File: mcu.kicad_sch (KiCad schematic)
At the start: 0 parts

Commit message: add ethernet
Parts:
- added U?: STM32F429ZGTx, Package_QFP:LQFP-144_20x20mm_P0.5mm, symbol MCU_ST_STM32F4:STM32F429ZGTx
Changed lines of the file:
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@@
 (kicad_sch (version 20211123) (generator eeschema)
   (paper "A3")
+  (symbol (lib_id "MCU_ST_STM32F4:STM32F429ZGTx") (at 199.39 143.51 0) (unit 1)
+    (in_bom yes) (on_board yes) (fields_autoplaced)
+    (property "Reference" "U?" (id 0) (at 214.1094 232.41 0)
+      (effects (font (size 1.27 1.27)) (justify left))
+    )
+    (property "Value" "STM32F429ZGTx" (id 1) (at 214.1094 234.95 0)
+      (effects (font (size 1.27 1.27)) (justify left))
+    )
+    (property "Footprint" "Package_QFP:LQFP-144_20x20mm_P0.5mm" (id 2) (at 173.99 229.87 0)
+      (effects (font (size 1.27 1.27)) (justify right) hide)
+    )
+    (property "Datasheet" "http://www.st.com/st-web-ui/static/active/en/resource/technical/document/datasheet/DM00071990.pdf" (id 3) (at 199.39 143.51 0)
+      (effects (font (size 1.27 1.27)) hide)
+    )
+    (pin "1")
+    (pin "10")
+    (pin "100")
+    (pin "101")
+    (pin "102")
+    (pin "103")
+    (pin "104")
+    (pin "105")
+    (pin "106")
+    (pin "107")
+    (pin "108")
+    (pin "109")
+    (pin "11")
+    (pin "110")
+    (pin "111")
+    (pin "112")
+    (pin "113")
+    (pin "114")
+    (pin "115")
+    (pin "116")
+    (pin "117")
+    (pin "118")
+    (pin "119")
+    (pin "12")
+    (pin "120")
+    (pin "121")
+    (pin "122")
+    (pin "123")
+    (pin "124")
+    (pin "125")
+    (pin "126")
+    (pin "127")
+    (pin "128")
+    (pin "129")
+    (pin "13")
+    (pin "130")
+    (pin "131")
+    (pin "132")
+    (pin "133")
+    (pin "134")
+    (pin "135")
+    (pin "136")
+    (pin "137")
+    (pin "138")
+    (pin "139")
+    (pin "14")
+    (pin "140")
+    (pin "141")
+    (pin "142")
+    (pin "143")
+    (pin "144")
+    (pin "15")
+    (pin "16")
+    (pin "17")
+    (pin "18")
+    (pin "19")
+    (pin "2")
+    (pin "20")
+    (pin "21")
+    (pin "22")
+    (pin "23")
+    (pin "24")
+    (pin "25")
+    (pin "26")
+    (pin "27")
+    (pin "28")
+    (pin "29")
+    (pin "3")
+    (pin "30")
+    (pin "31")
+    (pin "32")
+    (pin "33")
+    (pin "34")
+    (pin "35")
+    (pin "36")
+    (pin "37")
+    (pin "38")
+    (pin "39")
+    (pin "4")
+    (pin "40")
+    (pin "41")
+    (pin "42")
+    (pin "43")
+    (pin "44")
+    (pin "45")
+    (pin "46")
+    (pin "47")
+    (pin "48")
+    (pin "49")
+    (pin "5")
+    (pin "50")
+    (pin "51")
+    (pin "52")
+    (pin "53")
+    (pin "54")
+    (pin "55")
+    (pin "56")
+    (pin "57")
+    (pin "58")
+    (pin "59")
+    (pin "6")
+    (pin "60")
+    (pin "61")
+    (pin "62")
+    (pin "63")
+    (pin "64")
+    (pin "65")
+    (pin "66")
+    (pin "67")
+    (pin "68")
+    (pin "69")
+    (pin "7")
+    (pin "70")
+    (pin "71")
+    (pin "72")
+    (pin "73")
+    (pin "74")
+    (pin "75")
+    (pin "76")
+    (pin "77")
+    (pin "78")
+    (pin "79")
+    (pin "8")
+    (pin "80")
+    (pin "81")
+    (pin "82")
+    (pin "83")
+    (pin "84")
+    (pin "85")
+    (pin "86")
+    (pin "87")
+    (pin "88")
+    (pin "89")
+    (pin "9")
+    (pin "90")
+    (pin "91")
+    (pin "92")
+    (pin "93")
+    (pin "94")
+    (pin "95")
+    (pin "96")
+    (pin "97")
+    (pin "98")
+    (pin "99")
+  )
 )

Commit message: add USB
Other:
- company: (none) -> M-Labs
- title: (none) -> Kirdy
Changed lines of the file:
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@@
 (kicad_sch (version 20211123) (generator eeschema)
   (paper "A3")
+  (title_block
+    (title "Kirdy")
+    (date "2022-07-03")
+    (rev "r0.1")
+    (company "M-Labs")
+    (comment 1 "Alex Wong Tat Hang")
+  )
   (symbol (lib_id "MCU_ST_STM32F4:STM32F429ZGTx") (at 199.39 143.51 0) (unit 1)
     (in_bom yes) (on_board yes) (fields_autoplaced)

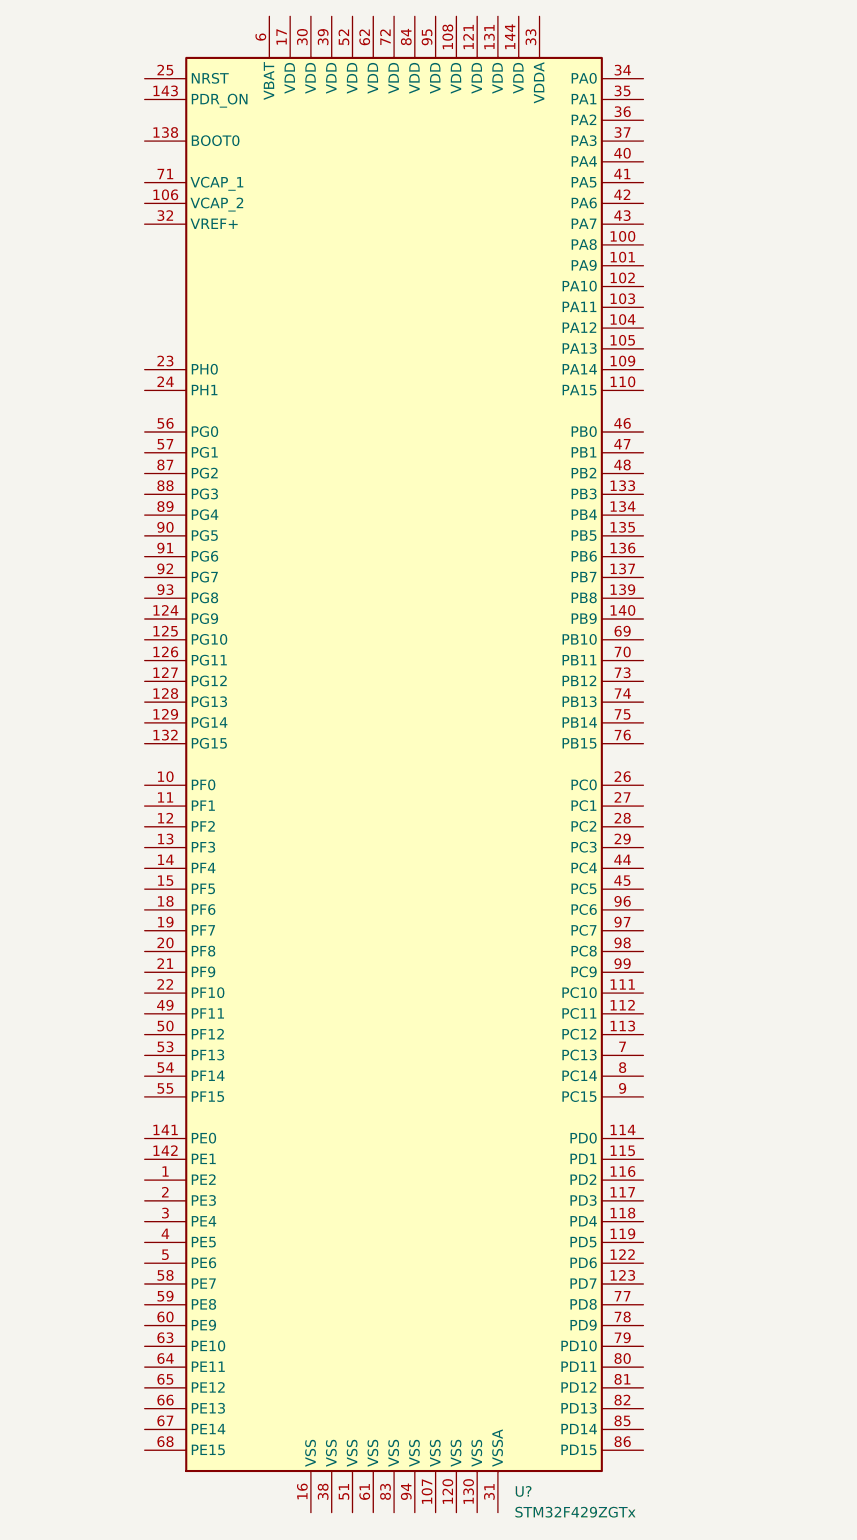
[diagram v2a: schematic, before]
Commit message: add MCU basic connections
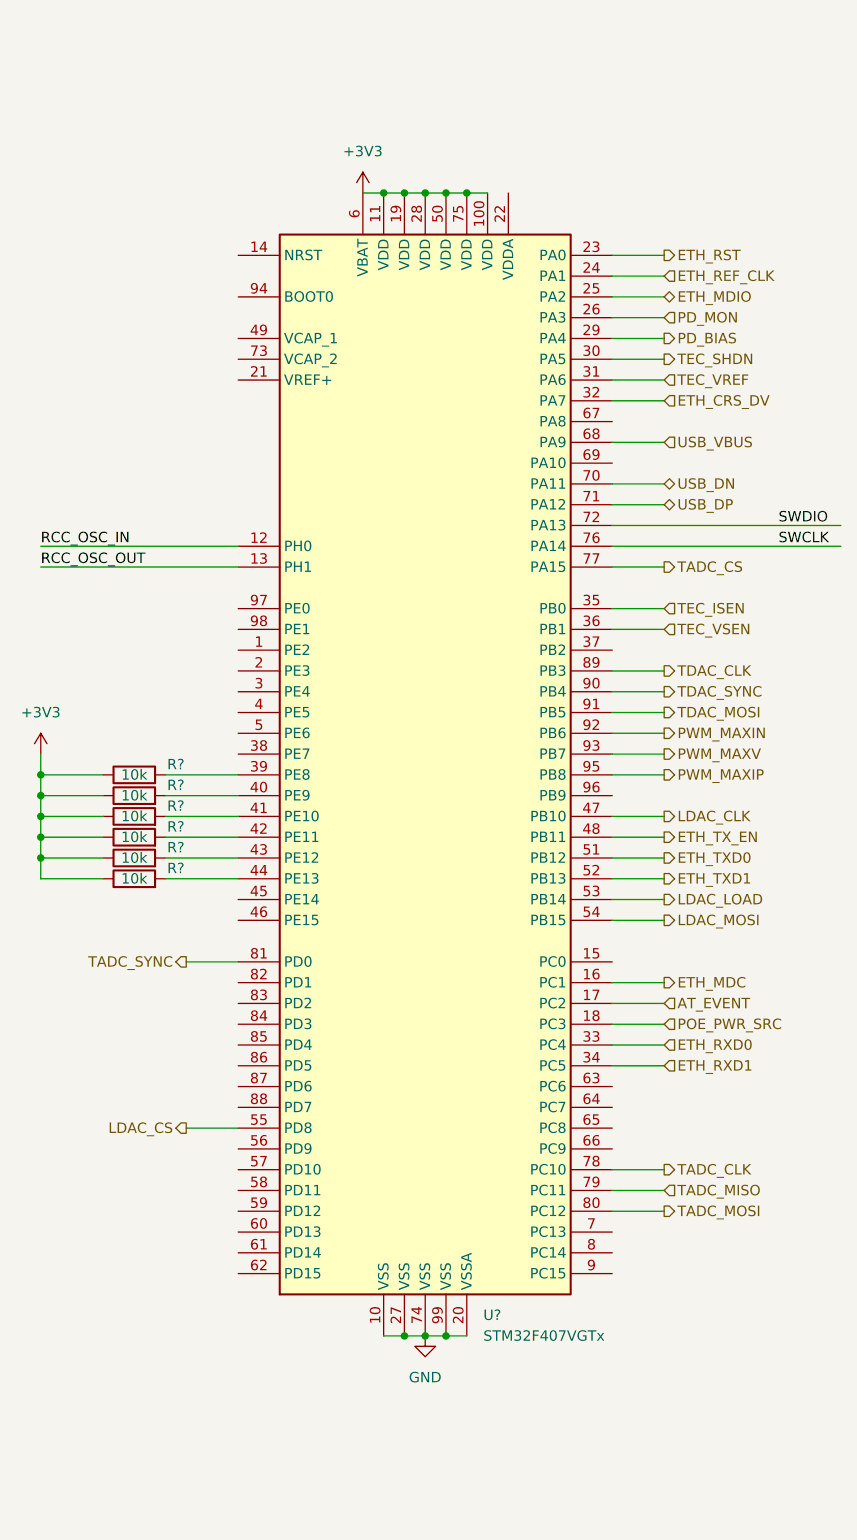
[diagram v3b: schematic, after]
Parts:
- removed U?: STM32F429ZGTx, Package_QFP:LQFP-144_20x20mm_P0.5mm, symbol MCU_ST_STM32F4:STM32F429ZGTx
- added R? (x6): 10k, symbol Device:R
- added U?: STM32F407VGTx, Package_QFP:LQFP-100_14x14mm_P0.5mm, symbol MCU_ST_STM32F4:STM32F407VGTx
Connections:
- new net: R?.2, U?.41 (PE10)
- new net: R?.2, U?.39 (PE8)
- new net: R?.2, U?.40 (PE9)
- new net: R?.2, U?.42 (PE11)
- new net: R?.2, U?.43 (PE12)
- new net: R?.2, U?.44 (PE13)
- new net +3V3: R?.1, R?.1, R?.1, R?.1, R?.1, R?.1, U?.100 (VDD), U?.11 (VDD), U?.19 (VDD), U?.28 (VDD), U?.50 (VDD), U?.6 (VBAT), U?.75 (VDD)
- new net AT_EVENT: U?.17 (PC2)
- new net ETH_CRS_DV: U?.32 (PA7)
- new net ETH_MDC: U?.16 (PC1)
- new net ETH_MDIO: U?.25 (PA2)
- new net ETH_REF_CLK: U?.24 (PA1)
- new net ETH_RST: U?.23 (PA0)
- new net ETH_RXD0: U?.33 (PC4)
- new net ETH_RXD1: U?.34 (PC5)
- new net ETH_TXD0: U?.51 (PB12)
- new net ETH_TXD1: U?.52 (PB13)
- new net ETH_TX_EN: U?.48 (PB11)
- new net GND: U?.10 (VSS), U?.20 (VSSA), U?.27 (VSS), U?.74 (VSS), U?.99 (VSS)
- new net LDAC_CLK: U?.47 (PB10)
- new net LDAC_CS: U?.55 (PD8)
- new net LDAC_LOAD: U?.53 (PB14)
- new net LDAC_MOSI: U?.54 (PB15)
- new net PD_BIAS: U?.29 (PA4)
- new net PD_MON: U?.26 (PA3)
- new net POE_PWR_SRC: U?.18 (PC3)
- new net PWM_MAXIN: U?.92 (PB6)
- new net PWM_MAXIP: U?.95 (PB8)
- new net PWM_MAXV: U?.93 (PB7)
- new net RCC_OSC_IN: U?.12 (PH0)
- new net RCC_OSC_OUT: U?.13 (PH1)
- new net SWCLK: U?.76 (PA14)
- new net SWDIO: U?.72 (PA13)
- new net TADC_CLK: U?.78 (PC10)
- new net TADC_CS: U?.77 (PA15)
- new net TADC_MISO: U?.79 (PC11)
- new net TADC_MOSI: U?.80 (PC12)
- new net TADC_SYNC: U?.81 (PD0)
- new net TDAC_CLK: U?.89 (PB3)
- new net TDAC_MOSI: U?.91 (PB5)
- new net TDAC_SYNC: U?.90 (PB4)
- new net TEC_ISEN: U?.35 (PB0)
- new net TEC_SHDN: U?.30 (PA5)
- new net TEC_VREF: U?.31 (PA6)
- new net TEC_VSEN: U?.36 (PB1)
- new net USB_DN: U?.70 (PA11)
- new net USB_DP: U?.71 (PA12)
- new net USB_VBUS: U?.68 (PA9)

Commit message: complete mcu
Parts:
- added C18, C19, C20, C29: 2u2, symbol Device:C
- added C21, C22: 12p, symbol Device:C
- added C23, C24, C25, C26, C27, C28, C30, C31: 100n, symbol Device:C
- added D3: B5819, symbol Device:D_Shockley
- added FB1: 1K@100MHz, symbol Device:FerriteBead_Small
- added J4: Conn_02x05_Odd_Even, symbol Connector_Generic:Conn_02x05_Odd_Even
- added JP1: Jumper_2_Open, symbol Jumper:Jumper_2_Open
- added R20, R21: 10k, symbol Device:R
- added U8: STM809SWX6F, Package_TO_SOT_SMD:SOT-23, symbol kirdy:STM809SWX6F
- added Y1: 8MHz, symbol Device:Crystal
- gave numbers to parts that had none: 7
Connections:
- net +3V3: now also C20.1, C23.1, C24.1, C25.1, C26.1, C27.1, C30.1, C31.1, FB1.1, J4.1 (Pin_1), JP1.2 (B), R21.1, U8.3 (VCC)
- net GND: now also C18.2, C19.2, C20.2, C21.1, C22.2, C23.2, C24.2, C25.2, C26.2, C27.2, C28.2, C29.2, C30.2, C31.2, J4.3 (Pin_3), J4.5 (Pin_5), R20.1, U8.1 (VSS)
- net SWCLK: now also J4.4 (Pin_4)
- net SWDIO: now also J4.2 (Pin_2)
- net RST: now reaches U7.14 (NRST)
- net RST: now also D3.2 (A), R21.2
- net VREF: now reaches U7.21 (VREF+)
- net VREF: now also U7.22 (VDDA), C28.1, C29.1, FB1.2
- net at U7.49 (VCAP_1): now also C18.1
- net at U7.73 (VCAP_2): now also C19.1
- net at U7.94 (BOOT0): now also R20.2
- net RCC_OSC_IN: no longer names the net of U7.12 (PH0)
- net RCC_OSC_IN: now also C21.2, Y1.2
- net RCC_OSC_OUT: no longer names the net of U7.13 (PH1)
- net RCC_OSC_OUT: now also C22.1, Y1.1
- new net MCU_RSTn: D3.1 (K), U8.2 (RST)
- no-connect marks 0 -> 39
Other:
- note added: "Revision"
- moved on the sheet: R14, R15, R16, R17, R18, R19

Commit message: first draft complete
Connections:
- net RST: now also J4.10 (Pin_10)
- net at JP1.1 (A): now also R20.2, U7.94 (BOOT0)
- no-connect marks 39 -> 40
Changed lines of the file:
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@@
   (junction (at 198.12 73.66) (diameter 0) (color 0 0 0 0)
   )
+  (junction (at 157.48 93.98) (diameter 0) (color 0 0 0 0)
+  )
   (junction (at 205.74 213.36) (diameter 0) (color 0 0 0 0)
   )
@@
   (junction (at 203.2 213.36) (diameter 0) (color 0 0 0 0)
   )
+  (junction (at 175.26 96.52) (diameter 0) (color 0 0 0 0)
+  )
   (junction (at 204.47 38.1) (diameter 0) (color 0 0 0 0)
   )
+  (junction (at 152.4 86.36) (diameter 0) (color 0 0 0 0)
+  )
   (junction (at 113.03 154.94) (diameter 0) (color 0 0 0 0)
   )
@@
   )
   (junction (at 200.66 213.36) (diameter 0) (color 0 0 0 0)
+  )
+  (junction (at 157.48 91.44) (diameter 0) (color 0 0 0 0)
   )
   (junction (at 208.28 73.66) (diameter 0) (color 0 0 0 0)
@@
   (no_connect (at 325.12 93.98))
   (no_connect (at 325.12 91.44))
+  (no_connect (at 312.42 93.98))
   (no_connect (at 180.34 198.12))
   (no_connect (at 180.34 200.66))
@@
     (stroke (width 0) (type default) (color 0 0 0 0))
   )
+  (wire (pts (xy 175.26 96.52) (xy 180.34 96.52))
+    (stroke (width 0) (type default) (color 0 0 0 0))
+  )
   (wire (pts (xy 198.12 213.36) (xy 200.66 213.36))
     (stroke (width 0) (type default) (color 0 0 0 0))
@@
     (stroke (width 0) (type default) (color 0 0 0 0))
   )
+  (wire (pts (xy 157.48 93.98) (xy 180.34 93.98))
+    (stroke (width 0) (type default) (color 0 0 0 0))
+  )
   (wire (pts (xy 314.96 113.03) (xy 326.39 113.03))
     (stroke (width 0) (type default) (color 0 0 0 0))
@@
     (stroke (width 0) (type default) (color 0 0 0 0))
   )
-  (wire (pts (xy 133.35 93.98) (xy 180.34 93.98))
+  (wire (pts (xy 133.35 93.98) (xy 157.48 93.98))
     (stroke (width 0) (type default) (color 0 0 0 0))
   )
@@
     (stroke (width 0) (type default) (color 0 0 0 0))
   )
+  (wire (pts (xy 152.4 86.36) (xy 180.34 86.36))
+    (stroke (width 0) (type default) (color 0 0 0 0))
+  )
   (wire (pts (xy 198.12 73.66) (xy 200.66 73.66))
     (stroke (width 0) (type default) (color 0 0 0 0))
@@
     (stroke (width 0) (type default) (color 0 0 0 0))
   )
-  (wire (pts (xy 165.1 96.52) (xy 180.34 96.52))
+  (wire (pts (xy 165.1 96.52) (xy 175.26 96.52))
     (stroke (width 0) (type default) (color 0 0 0 0))
   )
@@
     (stroke (width 0) (type default) (color 0 0 0 0))
   )
+  (wire (pts (xy 157.48 91.44) (xy 180.34 91.44))
+    (stroke (width 0) (type default) (color 0 0 0 0))
+  )
   (wire (pts (xy 226.06 109.22) (xy 232.41 109.22))
     (stroke (width 0) (type default) (color 0 0 0 0))
@@
     (stroke (width 0) (type default) (color 0 0 0 0))
   )
-  (wire (pts (xy 143.51 86.36) (xy 180.34 86.36))
+  (wire (pts (xy 143.51 86.36) (xy 152.4 86.36))
     (stroke (width 0) (type default) (color 0 0 0 0))
   )
@@
     (stroke (width 0) (type default) (color 0 0 0 0))
   )
-  (wire (pts (xy 121.92 91.44) (xy 180.34 91.44))
+  (wire (pts (xy 121.92 91.44) (xy 157.48 91.44))
     (stroke (width 0) (type default) (color 0 0 0 0))
   )
@@
   )
   (label "RST" (at 345.44 133.35 0)
+    (effects (font (size 1.27 1.27)) (justify left bottom))
+  )
+  (label "RST" (at 335.28 96.52 0)
     (effects (font (size 1.27 1.27)) (justify left bottom))
   )
@@
     (pin "1")
     (pin "2")
+  )
+  (symbol (lib_id "power:PWR_FLAG") (at 157.48 93.98 180) (unit 1)
+    (in_bom yes) (on_board yes) (fields_autoplaced)
+    (property "Reference" "#FLG04" (id 0) (at 157.48 95.885 0)
+      (effects (font (size 1.27 1.27)) hide)
+    )
+    (property "Value" "PWR_FLAG" (id 1) (at 157.48 99.06 0)
+      (effects (font (size 1.27 1.27)) hide)
+    )
+    (property "Footprint" "" (id 2) (at 157.48 93.98 0)
+      (effects (font (size 1.27 1.27)) hide)
+    )
+    (property "Datasheet" "~" (id 3) (at 157.48 93.98 0)
+      (effects (font (size 1.27 1.27)) hide)
+    )
+    (pin "1")
   )
   (symbol (lib_id "MCU_ST_STM32F4:STM32F407VGTx") (at 203.2 142.24 0) (unit 1)
@@
     (pin "2")
   )
+  (symbol (lib_id "power:PWR_FLAG") (at 157.48 91.44 0) (unit 1)
+    (in_bom yes) (on_board yes) (fields_autoplaced)
+    (property "Reference" "#FLG03" (id 0) (at 157.48 89.535 0)
+      (effects (font (size 1.27 1.27)) hide)
+    )
+    (property "Value" "PWR_FLAG" (id 1) (at 157.48 86.36 0)
+      (effects (font (size 1.27 1.27)) hide)
+    )
+    (property "Footprint" "" (id 2) (at 157.48 91.44 0)
+      (effects (font (size 1.27 1.27)) hide)
+    )
+    (property "Datasheet" "~" (id 3) (at 157.48 91.44 0)
+      (effects (font (size 1.27 1.27)) hide)
+    )
+    (pin "1")
+  )
   (symbol (lib_id "power:+3V3") (at 113.03 142.24 0) (unit 1)
     (in_bom yes) (on_board yes) (fields_autoplaced)
@@
       (effects (font (size 1.27 1.27)) hide)
     )
+    (pin "1")
+  )
+  (symbol (lib_id "power:PWR_FLAG") (at 175.26 96.52 180) (unit 1)
+    (in_bom yes) (on_board yes) (fields_autoplaced)
+    (property "Reference" "#FLG05" (id 0) (at 175.26 98.425 0)
+      (effects (font (size 1.27 1.27)) hide)
+    )
+    (property "Value" "PWR_FLAG" (id 1) (at 175.26 101.6 0)
+      (effects (font (size 1.27 1.27)) hide)
+    )
+    (property "Footprint" "" (id 2) (at 175.26 96.52 0)
+      (effects (font (size 1.27 1.27)) hide)
+    )
+    (property "Datasheet" "~" (id 3) (at 175.26 96.52 0)
+      (effects (font (size 1.27 1.27)) hide)
+    )

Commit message: Complete BOM, FP assignment
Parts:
- C18, C19, C20, C29: footprint (none) -> Capacitor_SMD:C_0603_1608Metric; MFR_PN (none) -> CL10B225KP8NNNC; MFR_PN_ALT (none) -> CGA3E1X7R0J225K080AC
- C21, C22: footprint (none) -> Capacitor_SMD:C_0603_1608Metric; MFR_PN (none) -> 0603N120J500CT; MFR_PN_ALT (none) -> C0603C120K5HAC7867
- C23, C24, C25, C26, C27, C28, C30, C31: footprint (none) -> Capacitor_SMD:C_0603_1608Metric; MFR_PN (none) -> CL10B104KB8NNWC; MFR_PN_ALT (none) -> CL10B104KB8NNNL
- D3: footprint (none) -> Diode_SMD:D_SOD-323; MFR_PN (none) -> B5819WS-TP
- FB1: footprint (none) -> Inductor_SMD:L_1210_3225Metric; MFR_PN (none) -> FBMH3225HM102NT; MFR_PN_ALT (none) -> FBMH3225HM102NTV
- J4: footprint (none) -> Connector_PinHeader_1.27mm:PinHeader_2x05_P1.27mm_Vertical_SMD; MFR_PN (none) -> M50-3600542
- JP1: value Jumper_2_Open -> DNP; footprint (none) -> Connector_PinHeader_2.54mm:PinHeader_1x02_P2.54mm_Vertical
- R14, R15, R16, R17, R18, R19, R20, R21: footprint (none) -> Resistor_SMD:R_0603_1608Metric; MFR_PN (none) -> RNCP0603FTD10K0; MFR_PN_ALT (none) -> RMCF0603FT10K0
- U7: MFR_PN (none) -> STM32F407VGT6
- U8: MFR_PN (none) -> STM809SWX6F
- Y1: footprint (none) -> Crystal:Crystal_SMD_5032-2Pin_5.0x3.2mm; MFR_PN (none) -> ECS-80-12-30Q-DS-TR; MFR_PN_ALT (none) -> ECS-80-12-30-JGN-TR
